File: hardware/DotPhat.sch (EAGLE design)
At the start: 39 parts, among them CN1 1X4-BIG, IC1 CAT24M010TS, J2 RASPBERRYPI-40-PIN-GPIO_PTH, J3 USB-MICROB, U1 ATMEGA328P-MU-QFN32, U2 TMP102, U3 ATSHA204-TSU, X3 S4B-ZR

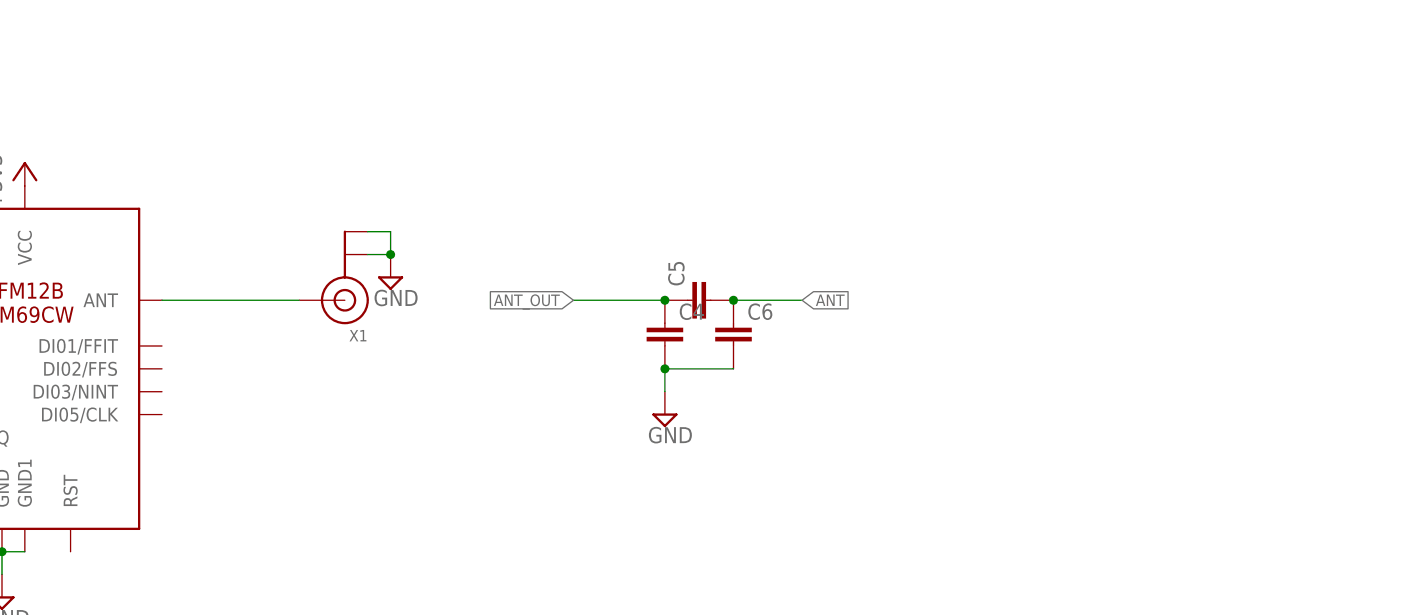
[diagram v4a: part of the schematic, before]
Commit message: Reposition antenna PI-filter
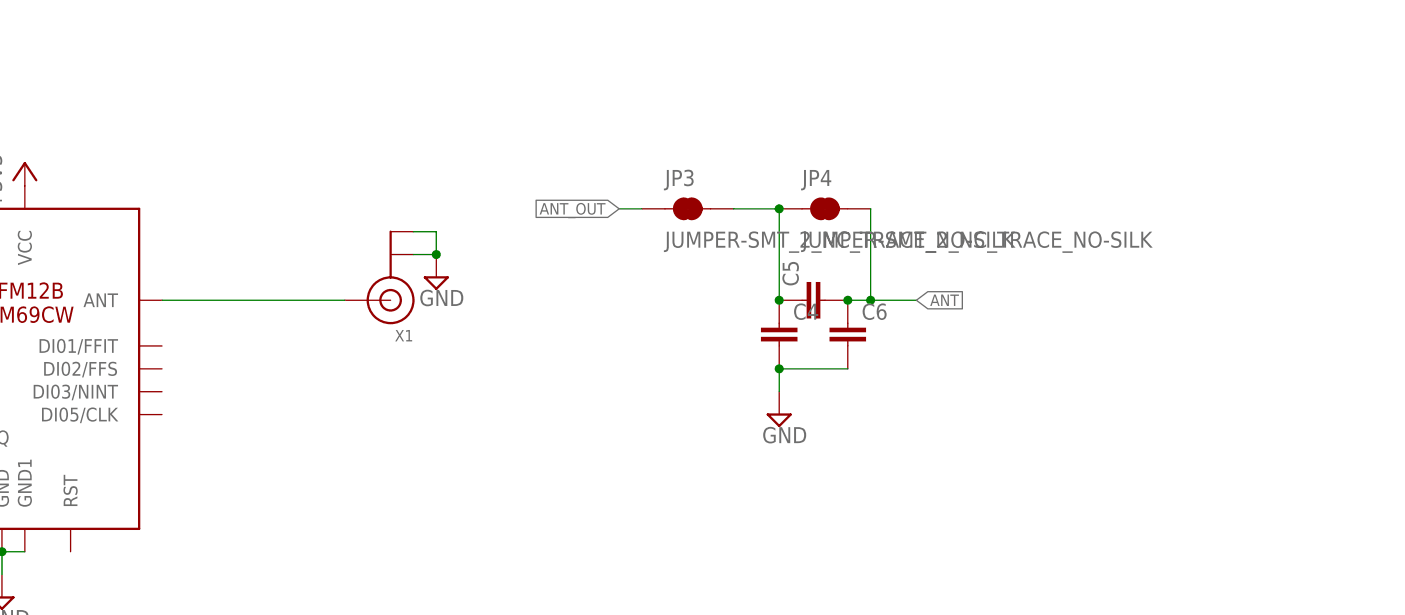
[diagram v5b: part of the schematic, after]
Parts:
- added JP3, JP4: JUMPER-SMT_2_NC_TRACE_NO-SILK, SparkFun-Jumpers:JUMPER-SMT_2_NC_TRACE_NO-SILK
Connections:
- new net N$3: C4.1, C5.1, JP3.2, JP4.1
- net ANT: now also JP4.2
- net ANT_OUT: now also JP3.1; no longer C4.1, C5.1
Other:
- moved on the sheet: C4, C5, C6, X1
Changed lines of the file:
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@@
 <part name="SPK1" library="adafruit" deviceset="SMT-0540-S-R" device=""/>
 <part name="SUPPLY22" library="supply2" deviceset="GND" device=""/>
+<part name="JP3" library="SparkFun-Jumpers" deviceset="JUMPER-SMT_2_NC_TRACE" device="_NO-SILK"/>
+<part name="JP4" library="SparkFun-Jumpers" deviceset="JUMPER-SMT_2_NC_TRACE" device="_NO-SILK"/>
 </parts>
 <sheets>
@@
 <instance part="+3V4" gate="G$1" x="27.94" y="58.42"/>
 <instance part="+3V5" gate="G$1" x="142.24" y="86.36"/>
-<instance part="X1" gate="G$1" x="177.8" y="71.12" rot="R180"/>
-<instance part="SUPPLY5" gate="GND" x="182.88" y="73.66"/>
+<instance part="X1" gate="G$1" x="182.88" y="71.12" rot="R180"/>
+<instance part="SUPPLY5" gate="GND" x="187.96" y="73.66"/>
 <instance part="+3V2" gate="G$1" x="22.86" y="78.74" rot="R90"/>
 <instance part="Y1" gate="G$1" x="81.28" y="68.58" rot="R90"/>
@@
 <instance part="+3V15" gate="G$1" x="142.24" y="-81.28"/>
 <instance part="SUPPLY20" gate="GND" x="142.24" y="-93.98"/>
-<instance part="C4" gate="G$1" x="213.36" y="68.58"/>
-<instance part="C5" gate="G$1" x="215.9" y="71.12" rot="R90"/>
-<instance part="C6" gate="G$1" x="220.98" y="68.58"/>
-<instance part="SUPPLY21" gate="GND" x="213.36" y="58.42"/>
+<instance part="C4" gate="G$1" x="226.06" y="68.58"/>
+<instance part="C5" gate="G$1" x="228.6" y="71.12" rot="R90"/>
+<instance part="C6" gate="G$1" x="233.68" y="68.58"/>
+<instance part="SUPPLY21" gate="GND" x="226.06" y="58.42"/>
 <instance part="Y2" gate="G$1" x="147.32" y="-121.92" rot="R90"/>
 <instance part="SUPPLY26" gate="GND" x="165.1" y="-124.46"/>
@@
 <instance part="SPK1" gate="G$1" x="-73.66" y="63.5" rot="R90"/>
 <instance part="SUPPLY22" gate="GND" x="-73.66" y="53.34" rot="MR0"/>
+<instance part="JP3" gate="G$1" x="215.9" y="81.28"/>
+<instance part="JP4" gate="G$1" x="231.14" y="81.28"/>
 </instances>
 <busses>
@@
 <pinref part="X1" gate="G$1" pin="GND@0"/>
 <pinref part="SUPPLY5" gate="GND" pin="GND"/>
-<wire x1="180.34" y1="76.2" x2="182.88" y2="76.2" width="0.1524" layer="91"/>
+<wire x1="185.42" y1="76.2" x2="187.96" y2="76.2" width="0.1524" layer="91"/>
 <pinref part="X1" gate="G$1" pin="GND@1"/>
-<wire x1="180.34" y1="78.74" x2="182.88" y2="78.74" width="0.1524" layer="91"/>
-<wire x1="182.88" y1="78.74" x2="182.88" y2="76.2" width="0.1524" layer="91"/>
-<junction x="182.88" y="76.2"/>
+<wire x1="185.42" y1="78.74" x2="187.96" y2="78.74" width="0.1524" layer="91"/>
+<wire x1="187.96" y1="78.74" x2="187.96" y2="76.2" width="0.1524" layer="91"/>
+<junction x="187.96" y="76.2"/>
 </segment>
 <segment>
@@
 <pinref part="C4" gate="G$1" pin="2"/>
 <pinref part="SUPPLY21" gate="GND" pin="GND"/>
-<wire x1="213.36" y1="63.5" x2="213.36" y2="60.96" width="0.1524" layer="91"/>
+<wire x1="226.06" y1="63.5" x2="226.06" y2="60.96" width="0.1524" layer="91"/>
 <pinref part="C6" gate="G$1" pin="2"/>
-<wire x1="220.98" y1="63.5" x2="213.36" y2="63.5" width="0.1524" layer="91"/>
-<junction x="213.36" y="63.5"/>
+<wire x1="233.68" y1="63.5" x2="226.06" y2="63.5" width="0.1524" layer="91"/>
+<junction x="226.06" y="63.5"/>
 </segment>
 <segment>
@@
 <net name="ANT_OUT" class="0">
 <segment>
-<pinref part="C4" gate="G$1" pin="1"/>
-<pinref part="C5" gate="G$1" pin="1"/>
-<wire x1="213.36" y1="71.12" x2="203.2" y2="71.12" width="0.1524" layer="91"/>
-<junction x="213.36" y="71.12"/>
-<label x="203.2" y="71.12" size="1.27" layer="95" rot="R180" xref="yes"/>
-</segment>
-<segment>
+<pinref part="X1" gate="G$1" pin="SIGNAL"/>
 <pinref part="U$1" gate="G$1" pin="ANT"/>
-<pinref part="X1" gate="G$1" pin="SIGNAL"/>
-<wire x1="157.48" y1="71.12" x2="172.72" y2="71.12" width="0.1524" layer="91"/>
+<wire x1="177.8" y1="71.12" x2="157.48" y2="71.12" width="0.1524" layer="91"/>
+</segment>
+<segment>
+<pinref part="JP3" gate="G$1" pin="1"/>
+<wire x1="210.82" y1="81.28" x2="208.28" y2="81.28" width="0.1524" layer="91"/>
+<label x="208.28" y="81.28" size="1.27" layer="95" rot="R180" xref="yes"/>
 </segment>
 </net>
@@
 <pinref part="C5" gate="G$1" pin="2"/>
 <pinref part="C6" gate="G$1" pin="1"/>
-<wire x1="220.98" y1="71.12" x2="228.6" y2="71.12" width="0.1524" layer="91"/>
-<junction x="220.98" y="71.12"/>
-<label x="228.6" y="71.12" size="1.27" layer="95" xref="yes"/>
+<wire x1="233.68" y1="71.12" x2="236.22" y2="71.12" width="0.1524" layer="91"/>
+<junction x="233.68" y="71.12"/>
+<label x="241.3" y="71.12" size="1.27" layer="95" xref="yes"/>
+<pinref part="JP4" gate="G$1" pin="2"/>
+<wire x1="236.22" y1="71.12" x2="241.3" y2="71.12" width="0.1524" layer="91"/>
+<wire x1="236.22" y1="81.28" x2="236.22" y2="71.12" width="0.1524" layer="91"/>
+<junction x="236.22" y="71.12"/>
 </segment>
 </net>
@@
 </segment>
 </net>
+<net name="N$3" class="0">
+<segment>
+<pinref part="C5" gate="G$1" pin="1"/>
+<pinref part="C4" gate="G$1" pin="1"/>
+<pinref part="JP3" gate="G$1" pin="2"/>
+<wire x1="220.98" y1="81.28" x2="226.06" y2="81.28" width="0.1524" layer="91"/>
+<wire x1="226.06" y1="81.28" x2="226.06" y2="71.12" width="0.1524" layer="91"/>
+<junction x="226.06" y="71.12"/>
+<pinref part="JP4" gate="G$1" pin="1"/>
+<junction x="226.06" y="81.28"/>
+</segment>
+</net>

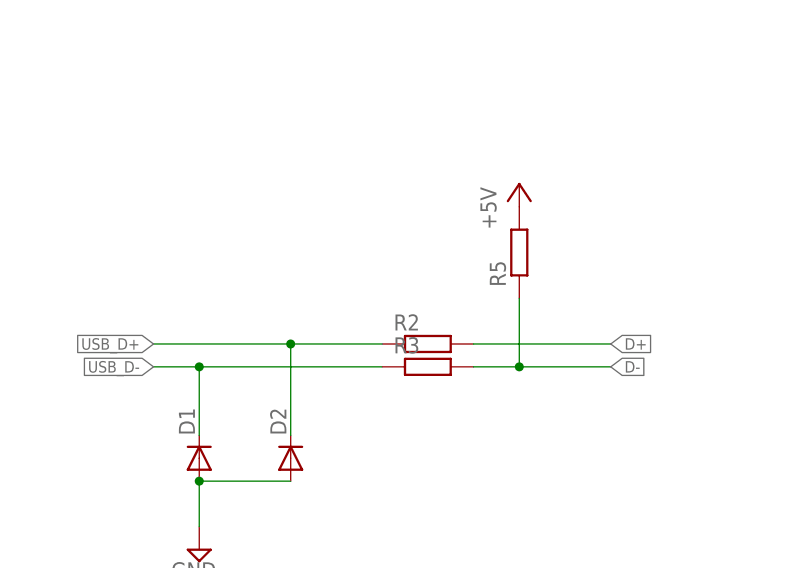
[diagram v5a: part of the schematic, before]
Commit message: Update USB pullup to downside, 3.3V instead of 5V
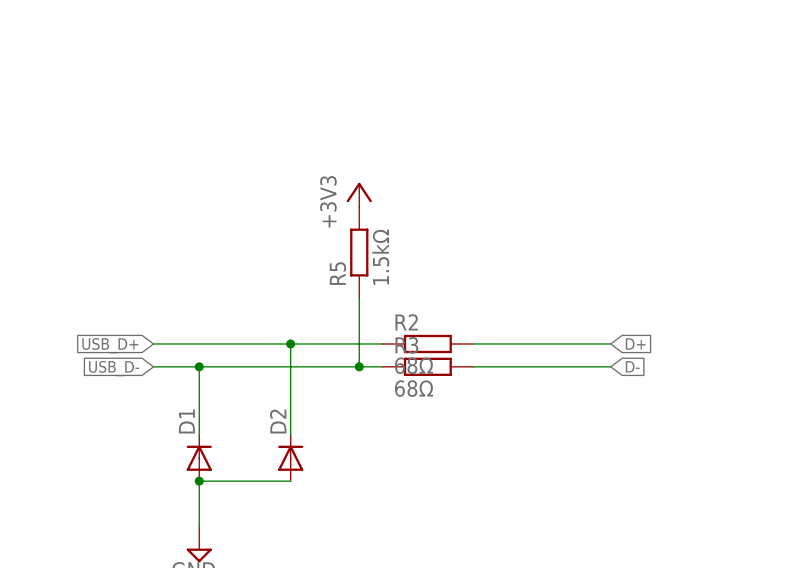
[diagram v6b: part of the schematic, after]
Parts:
- R2, R3: value (none) -> 68Ω
- R5: value (none) -> 1.5kΩ
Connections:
- net +3V3: now also R5.2
- net +5V: no longer R5.2
- net D-: no longer R5.1
- net USB_D-: now also R5.1
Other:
- moved on the sheet: R5
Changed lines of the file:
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@@
 <part name="D2" library="diode" deviceset="DIODE-" device="SOD523"/>
 <part name="SUPPLY14" library="supply2" deviceset="GND" device=""/>
-<part name="R2" library="rcl" deviceset="R-EU_" device="R0603"/>
-<part name="R3" library="rcl" deviceset="R-EU_" device="R0603"/>
-<part name="R5" library="rcl" deviceset="R-EU_" device="R0603"/>
-<part name="P+5" library="supply1" deviceset="+5V" device=""/>
+<part name="R2" library="rcl" deviceset="R-EU_" device="R0603" value="68Ω"/>
+<part name="R3" library="rcl" deviceset="R-EU_" device="R0603" value="68Ω"/>
+<part name="R5" library="rcl" deviceset="R-EU_" device="R0603" value="1.5kΩ"/>
 <part name="SUPPLY16" library="supply2" deviceset="GND" device=""/>
 <part name="IC1" library="CAT24M01YI" deviceset="CAT24M01" device="TS" technology="0"/>
@@
 <part name="JP3" library="SparkFun-Jumpers" deviceset="JUMPER-SMT_2_NC_TRACE" device="_NO-SILK"/>
 <part name="JP4" library="SparkFun-Jumpers" deviceset="JUMPER-SMT_2_NC_TRACE" device="_NO-SILK"/>
+<part name="+3V16" library="supply1" deviceset="+3V3" device=""/>
 </parts>
 <sheets>
@@
 <instance part="R2" gate="G$1" x="261.62" y="-55.88"/>
 <instance part="R3" gate="G$1" x="261.62" y="-58.42"/>
-<instance part="R5" gate="G$1" x="271.78" y="-45.72" rot="R90"/>
-<instance part="P+5" gate="1" x="271.78" y="-38.1"/>
+<instance part="R5" gate="G$1" x="254" y="-45.72" rot="R90"/>
 <instance part="SUPPLY16" gate="GND" x="111.76" y="-170.18"/>
 <instance part="IC1" gate="G$1" x="93.98" y="-162.56"/>
@@
 <instance part="JP3" gate="G$1" x="215.9" y="81.28"/>
 <instance part="JP4" gate="G$1" x="231.14" y="81.28"/>
+<instance part="+3V16" gate="G$1" x="254" y="-38.1"/>
 </instances>
 <busses>
@@
 <pinref part="+3V15" gate="G$1" pin="+3V3"/>
 </segment>
+<segment>
+<pinref part="R5" gate="G$1" pin="2"/>
+<pinref part="+3V16" gate="G$1" pin="+3V3"/>
+</segment>
 </net>
 <net name="ADCENA" class="0">
@@
 <junction x="134.62" y="-35.56"/>
 </segment>
-<segment>
-<pinref part="R5" gate="G$1" pin="2"/>
-<pinref part="P+5" gate="1" pin="+5V"/>
-</segment>
 </net>
 <net name="N$7" class="0">
@@
 <wire x1="236.22" y1="-58.42" x2="231.14" y2="-58.42" width="0.1524" layer="91"/>
 <label x="231.14" y="-58.42" size="1.27" layer="95" rot="R180" xref="yes"/>
-<wire x1="236.22" y1="-58.42" x2="256.54" y2="-58.42" width="0.1524" layer="91"/>
+<wire x1="236.22" y1="-58.42" x2="254" y2="-58.42" width="0.1524" layer="91"/>
 <junction x="236.22" y="-58.42"/>
 <pinref part="R3" gate="G$1" pin="1"/>
+<pinref part="R5" gate="G$1" pin="1"/>
+<wire x1="254" y1="-58.42" x2="256.54" y2="-58.42" width="0.1524" layer="91"/>
+<wire x1="254" y1="-50.8" x2="254" y2="-58.42" width="0.1524" layer="91"/>
+<junction x="254" y="-58.42"/>
 </segment>
 </net>
@@
 <segment>
 <pinref part="R3" gate="G$1" pin="2"/>
-<wire x1="266.7" y1="-58.42" x2="271.78" y2="-58.42" width="0.1524" layer="91"/>
-<pinref part="R5" gate="G$1" pin="1"/>
-<wire x1="271.78" y1="-58.42" x2="281.94" y2="-58.42" width="0.1524" layer="91"/>
-<wire x1="271.78" y1="-50.8" x2="271.78" y2="-58.42" width="0.1524" layer="91"/>
-<junction x="271.78" y="-58.42"/>
+<wire x1="266.7" y1="-58.42" x2="281.94" y2="-58.42" width="0.1524" layer="91"/>
 <label x="281.94" y="-58.42" size="1.27" layer="95" xref="yes"/>
 </segment>

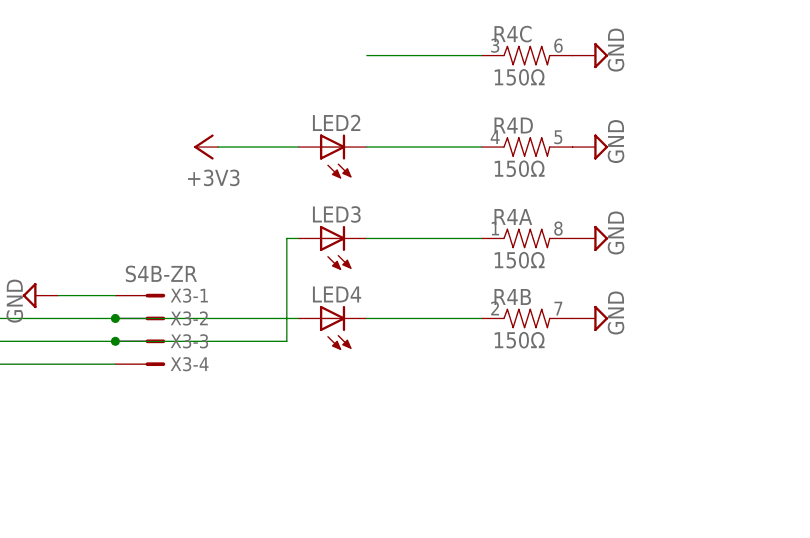
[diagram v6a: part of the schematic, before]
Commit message: Update actor leds' color in schematic
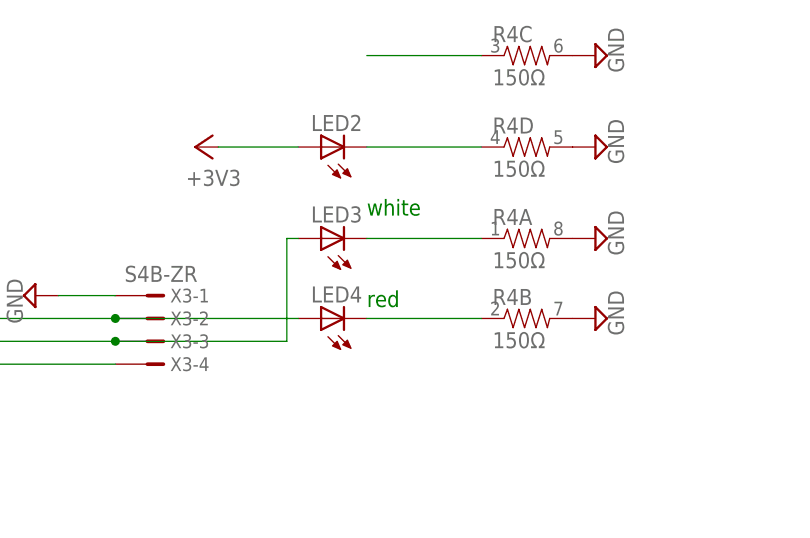
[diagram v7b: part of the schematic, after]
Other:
- note added: "red"
- note added: "white"
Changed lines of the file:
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@@
 <text x="228.6" y="20.32" size="1.016" layer="91" align="center">TMP102 or TMP112 (high acc +/-0.5°)</text>
 <text x="137.16" y="-147.32" size="3.81" layer="91">Authentification module</text>
+<text x="134.62" y="134.62" size="1.778" layer="91">white</text>
+<text x="134.62" y="124.46" size="1.778" layer="91">red</text>
 </plain>
 <instances>
